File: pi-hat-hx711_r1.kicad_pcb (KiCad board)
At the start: 2 copper layers, 65 x 56 mm, 15 parts, among them J1 GPIO, J2 Conn_01x06, J5 Conn_01x06, Q1 S8550, U2 HX711, U3 TPS7A20xxxDQN

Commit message: loloxoxlxoxl
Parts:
- added C1: 100nF, Capacitor_SMD:C_0603_1608Metric, F.Cu at (133.9, 73.8)
- added U1: M24c64, Package_SO:SOIC-8_3.9x4.9mm_P1.27mm, F.Cu at (140.5, 58.9)
- moved R3 21.8 mm to (138.8, 53.5)
- moved R1 21.2 mm to (138.5, 51.5)
- moved U3 11.0 mm to (151.0, 67.2)

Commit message: lollll
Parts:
- added C3: 10uF, Capacitor_SMD:C_0805_2012Metric, F.Cu at (141.8, 67.3)
- added C4: 100nF, Capacitor_SMD:C_0603_1608Metric, F.Cu at (133.0, 59.1)
- added C5: 100nF, Capacitor_SMD:C_0603_1608Metric, F.Cu at (133.0, 61.7)
- added D1: SS14, Diode_SMD:D_SMA, F.Cu at (139.0, 60.2)
- added JP2: Jumper_2_Open, TestPoint:TestPoint_2Pads_Pitch2.54mm_Drill0.8mm, F.Cu at (136.8, 64.1)
- added L1: 4u7H, Inductor_SMD:L_Sunlord_SWPA3015S, F.Cu at (137.3, 68.1)
- added R5: 100k, Resistor_SMD:R_0603_1608Metric, F.Cu at (133.0, 64.2)
- added R6: 360k, Resistor_SMD:R_0603_1608Metric, F.Cu at (133.0, 66.7)
- added U4: TPS61040DBV, Package_TO_SOT_SMD:SOT-23-5, F.Cu at (149.8, 55.5)
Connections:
- Q1 pad 3: unconnected-(Q1-C-Pad3) -> +VDC
- U2 pad 3: unconnected-(U2-AVDD-Pad3) -> +VDC
- U2 pad 5: unconnected-(U2-AGND-Pad5) -> -VDC
- U2 pad 6: unconnected-(U2-VBG-Pad6) -> Net-(U2-VBG)

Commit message: rough blocking out the pcb
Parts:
- removed JP2: Jumper_2_Open, TestPoint:TestPoint_2Pads_Pitch2.54mm_Drill0.8mm
- added C10: 1uF, Capacitor_SMD:C_0603_1608Metric, F.Cu at (112.0, 61.0)
- added C11: 22uF, Capacitor_SMD:C_0805_2012Metric, F.Cu at (108.0, 57.5)
- added C12: 33pF, Capacitor_SMD:C_0603_1608Metric, F.Cu at (116.0, 53.5)
- added C6: 22uF, Capacitor_SMD:C_0805_2012Metric, F.Cu at (109.0, 67.5)
- added C7: 22uF, Capacitor_SMD:C_0805_2012Metric, F.Cu at (109.0, 65.5)
- added C8: 1uF, Capacitor_SMD:C_0603_1608Metric, F.Cu at (115.0, 67.0)
- added C9: 33pF, Capacitor_SMD:C_0603_1608Metric, F.Cu at (140.8, 68.5)
- added JP1: ID_WP, Jumper:SolderJumper-2_P1.3mm_Open_TrianglePad1.0x1.5mm, F.Cu at (158.0, 58.5)
- added JP3: SolderJumper_2_Open, Jumper:SolderJumper-2_P1.3mm_Open_TrianglePad1.0x1.5mm, F.Cu at (103.5, 57.5)
- added R10: 0R, Resistor_SMD:R_0603_1608Metric, F.Cu at (144.8, 68.5)
- added R11: 10k, Resistor_SMD:R_0603_1608Metric, F.Cu at (144.8, 71.0)
- added R12: 0R, Resistor_SMD:R_0603_1608Metric, F.Cu at (148.8, 61.0)
- added R13: 10k, Resistor_SMD:R_0603_1608Metric, F.Cu at (148.8, 63.5)
- added R14: 3k9, Resistor_SMD:R_0603_1608Metric, F.Cu at (148.8, 66.0)
- added R15: 0R, Resistor_SMD:R_0603_1608Metric, F.Cu at (148.8, 68.5)
- added R7: 1R, Resistor_SMD:R_0603_1608Metric, F.Cu at (109.0, 63.5)
- added R8: 0R, Resistor_SMD:R_0603_1608Metric, F.Cu at (144.8, 63.5)
- added R9: 0R, Resistor_SMD:R_0603_1608Metric, F.Cu at (144.8, 66.0)
- added TP1: TestPoint, TestPoint:TestPoint_THTPad_1.5x1.5mm_Drill0.7mm, F.Cu at (145.0, 74.0)
- added TP2: TestPoint, TestPoint:TestPoint_THTPad_1.5x1.5mm_Drill0.7mm, F.Cu at (97.5, 64.5)
- added TP3: TestPoint, TestPoint:TestPoint_THTPad_1.5x1.5mm_Drill0.7mm, F.Cu at (96.0, 69.5)
- U3: value TPS7A20xxxDQN -> TPS7A2050PDQNR
- moved U4 38.8 mm to (111.0, 57.5), turned to -90 degrees
- moved U3 38.5 mm to (112.5, 67.5), turned to 180 degrees
- moved Q1 37.8 mm to (153.3, 73.7)
- moved R1 25.3 mm to (163.0, 58.0), turned to 180 degrees
- moved R3 24.9 mm to (163.0, 59.5), turned to 180 degrees
- moved L1 24.5 mm to (115.0, 58.0), turned to 90 degrees
- moved C1 24.4 mm to (156.5, 64.5), turned to -90 degrees
- moved R6 22.8 mm to (116.0, 51.5), turned to 180 degrees
- moved R5 22.6 mm to (113.0, 53.5), turned to 180 degrees
- moved U1 20.9 mm to (160.5, 64.9)
- moved D1 20.6 mm to (118.5, 59.0), turned to 90 degrees
- moved C4 8.93 mm to (140.8, 63.5)
- moved C5 8.93 mm to (140.8, 66.0)
- moved C3 6.54 mm to (141.0, 73.8)
- moved U2 5.91 mm to (130.5, 74.0), turned to 90 degrees
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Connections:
- net /IN1+ renamed /Analog/IN1+
- net /IN1- renamed /Analog/IN1-
- C3 pad 2: unconnected-(C3-Pad2) -> GND
- C4 pad 2: unconnected-(C4-Pad2) -> GND
- C5 pad 2: -VDC -> GND
- D1 pad 1: unconnected-(D1-K-Pad1) -> /power/VBOOST
- D1 pad 2: unconnected-(D1-A-Pad2) -> Net-(D1-A)
- J2 pad 1: -VDC -> GND
- J2 pad 2: -VDC -> /REFIN1-
- J2 pad 5: +VDC -> /REFIN1+
- J5 pad 2: +VDC -> /REFIN1+
- J5 pad 5: -VDC -> /REFIN1-
- J5 pad 6: -VDC -> GND
- L1 pad 1: unconnected-(L1-Pad1) -> +5V
- L1 pad 2: unconnected-(L1-Pad2) -> Net-(D1-A)
- Q1 pad 2: +5V -> Net-(Q1-E)
- R5 pad 1: unconnected-(R5-Pad1) -> Net-(U4-FB)
- R5 pad 2: unconnected-(R5-Pad2) -> GND
- R6 pad 1: unconnected-(R6-Pad1) -> /power/VBOOST
- R6 pad 2: unconnected-(R6-Pad2) -> Net-(U4-FB)
- U2 pad 1: +5V -> VDDA
- U2 pad 11: unconnected-(U2-PD_SCK-Pad11) -> /GPIO11/SPI0.SCLK
- U2 pad 12: unconnected-(U2-DOUT-Pad12) -> /GPIO9/SPI0.MISO
- U2 pad 14: unconnected-(U2-XI-Pad14) -> Net-(U2-XI)
- U2 pad 15: unconnected-(U2-RATE-Pad15) -> Net-(U2-RATE)
- U2 pad 2: Net-(Q1-B) -> Net-(U2-BASE)
- U2 pad 4: unconnected-(U2-VFB-Pad4) -> Net-(U2-VFB)
- U2 pad 5: -VDC -> GND
- U3 pad 1: unconnected-(U3-OUT-Pad1) -> VDDA
- U3 pad 2: unconnected-(U3-GND-Pad2) -> GND
- U3 pad 3: unconnected-(U3-EN-Pad3) -> Net-(U3-EN)
- U3 pad 4: unconnected-(U3-IN-Pad4) -> Net-(U3-EN)
- U3 pad 5: unconnected-(U3-Pad-Pad5) -> GND
- U4 pad 1: unconnected-(U4-SW-Pad1) -> Net-(D1-A)
- U4 pad 2: unconnected-(U4-GND-Pad2) -> GND
- U4 pad 3: unconnected-(U4-FB-Pad3) -> Net-(U4-FB)
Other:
- copper layers 2 -> 4

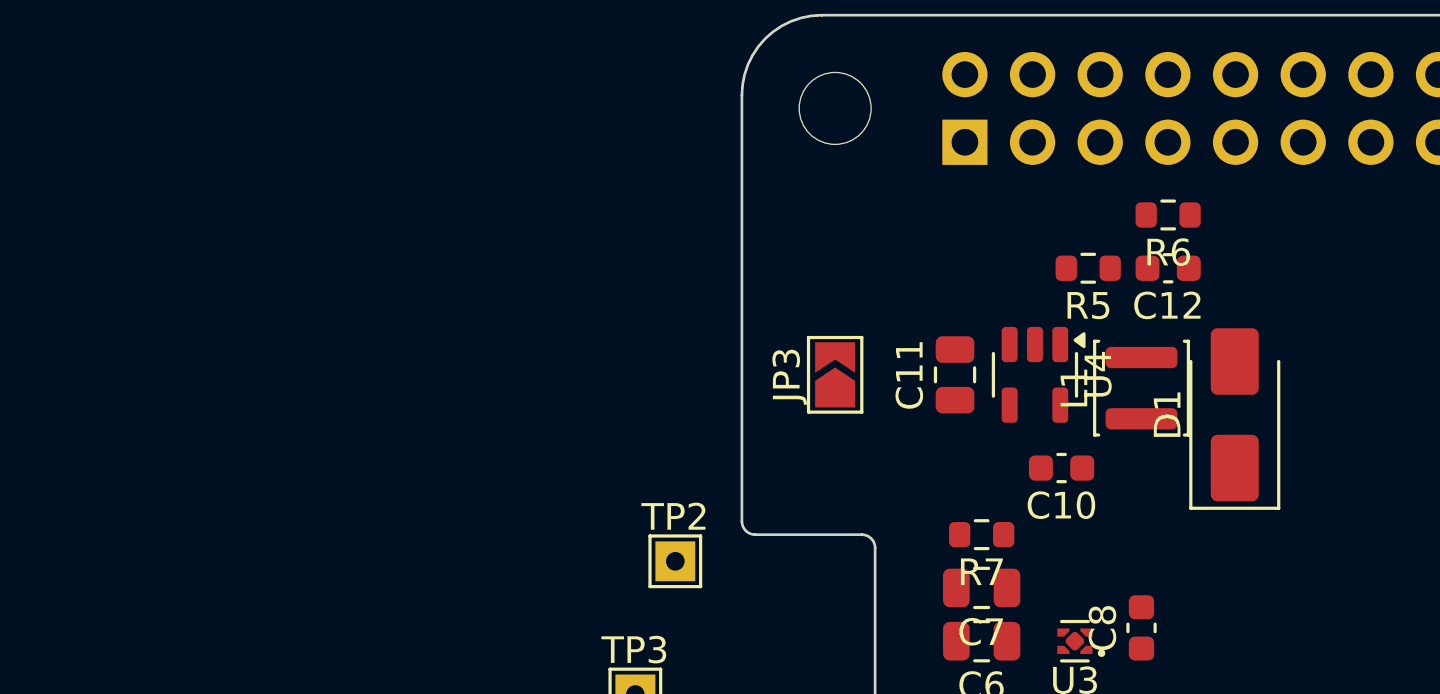
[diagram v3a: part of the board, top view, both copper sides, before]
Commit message: better parts, start pushing layout blocks
SMA is dumb, way too big
the swpa3030 was... unnecessarily small. we're trying to be super chill
power here, don't push it hot.  (Still, 1A was.. really, more than
enough? but 1A is a 40C rise, so.. let's just have less....)
use more caps too. why the fuck not. more filtering, more happy.

holy fuck though, kicad on wayland is giving me the shits!
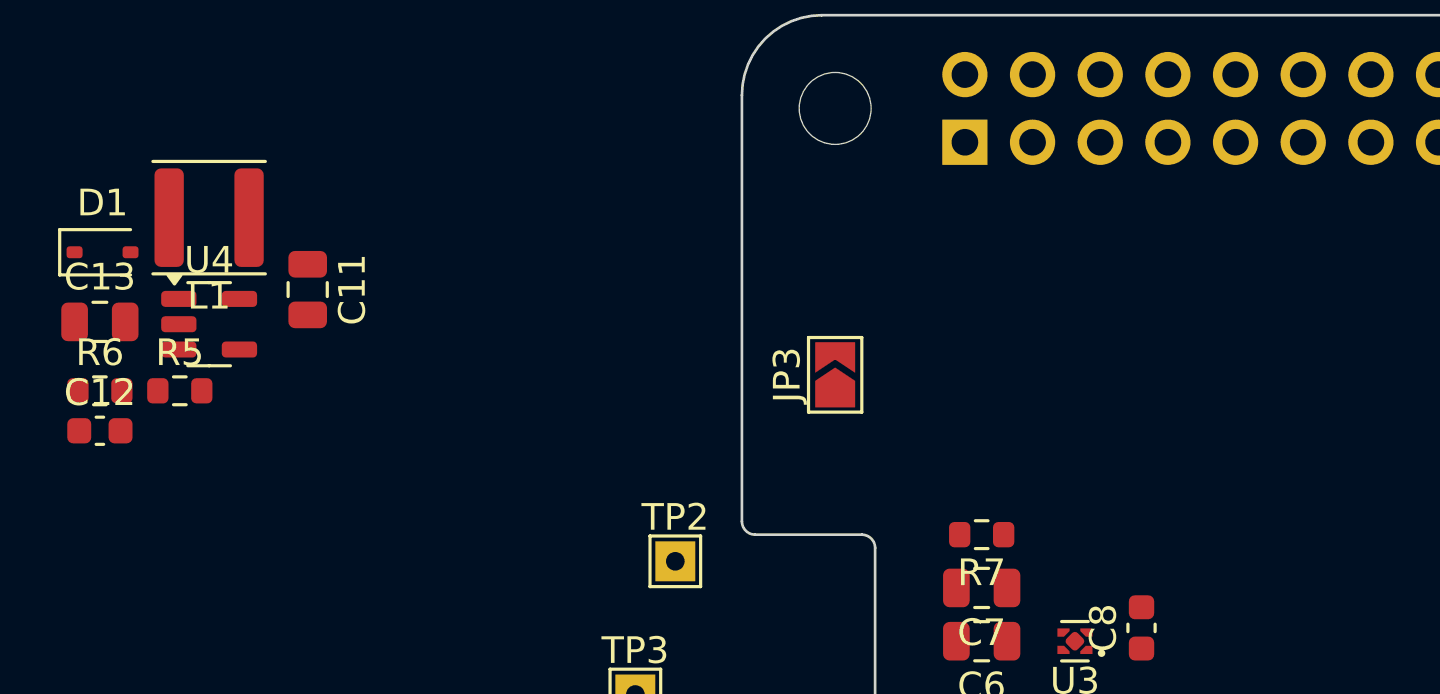
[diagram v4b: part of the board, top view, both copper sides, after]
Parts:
- removed C10: 1uF, Capacitor_SMD:C_0603_1608Metric
- added C13: 10uF, Capacitor_SMD:C_0805_2012Metric, F.Cu at (75.9, 55.5)
- D1: value SS14 -> 1N5819WS; footprint Diode_SMD:D_SMA -> Diode_SMD:D_SOD-323
- L1: footprint Inductor_SMD:L_Sunlord_SWPA3015S -> Inductor_SMD:L_Changjiang_FNR4030S
- moved D1 42.9 mm to (76.0, 52.9), turned to 0 degrees
- moved R6 40.6 mm to (75.9, 58.1), turned to 0 degrees
- moved C12 40.6 mm to (75.9, 59.6), turned to 0 degrees
- moved L1 35.6 mm to (80.0, 51.6), turned to 180 degrees
- moved R5 34.4 mm to (78.9, 58.1), turned to 0 degrees
- moved U4 31.1 mm to (80.0, 55.6), turned to 0 degrees
- moved C11 24.5 mm to (83.7, 54.3), turned to -90 degrees

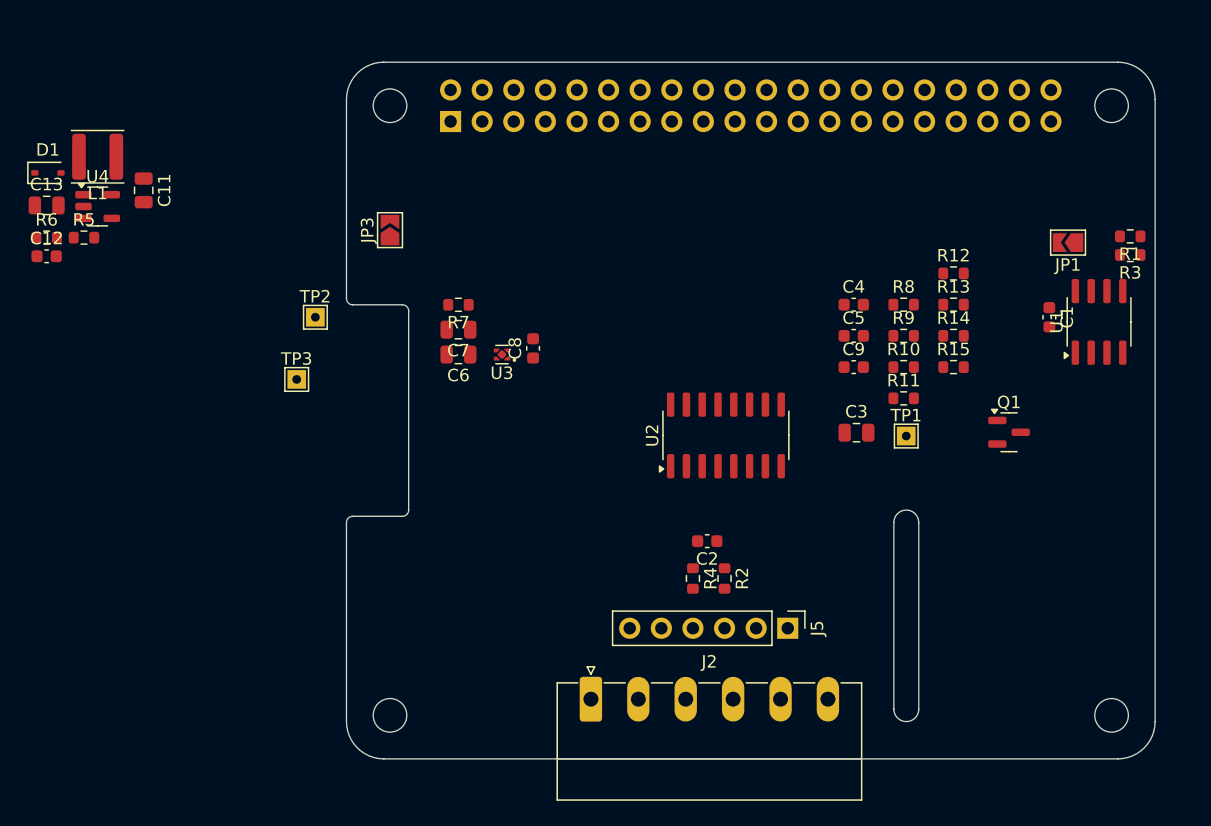
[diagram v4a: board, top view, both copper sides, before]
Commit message: add second channel input
switch to vertical connectors, so no concerns abotu edge space.
Allows offering the second channel, even though it's probably useless,
but it sets us up with a style we might be ok with for subsequent
boards.
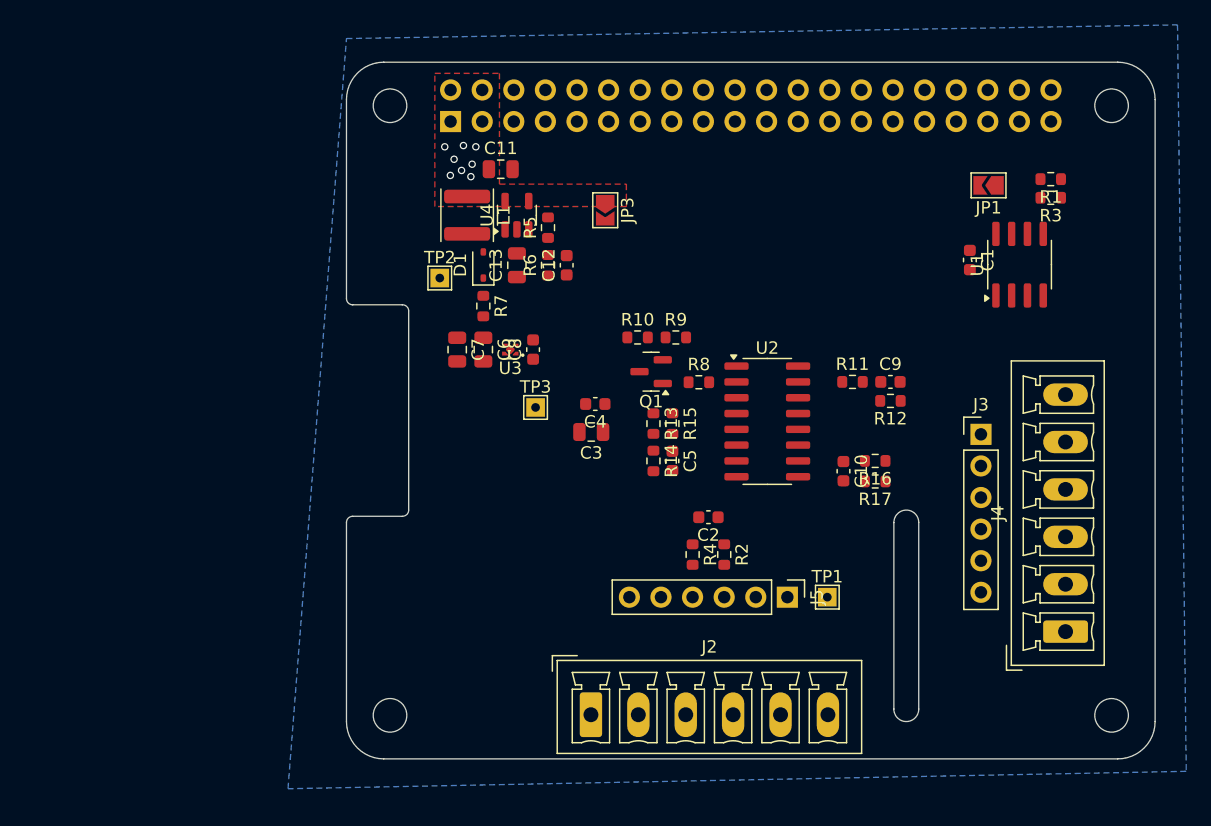
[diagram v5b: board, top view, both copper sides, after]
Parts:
- added C10: 100nF, Capacitor_SMD:C_0603_1608Metric, F.Cu at (139.9, 76.9)
- added J3: Conn_01x06, Connector_PinHeader_2.54mm:PinHeader_1x06_P2.54mm_Vertical, F.Cu at (151.0, 73.9)
- added J4: Conn_01x06, Connector_Phoenix_MC:PhoenixContact_MCV_1,5_6-G-3.81_1x06_P3.81mm_Vertical, F.Cu at (157.8, 89.8)
- added R16: 100R, Resistor_SMD:R_0603_1608Metric, F.Cu at (142.5, 76.0)
- added R17: 100R, Resistor_SMD:R_0603_1608Metric, F.Cu at (142.5, 77.7)
- J2: footprint Connector_Phoenix_MC:PhoenixContact_MC_1,5_6-G-3.81_1x06_P3.81mm_Horizontal -> Connector_Phoenix_MC:PhoenixContact_MCV_1,5_6-G-3.81_1x06_P3.81mm_Vertical
- moved C12 41.8 mm to (117.7, 60.3), turned to 90 degrees
- moved R6 40.4 mm to (116.2, 60.3), turned to 90 degrees
- moved C13 38.1 mm to (113.7, 60.3), turned to 90 degrees
- moved R5 37.3 mm to (116.2, 57.3), turned to 90 degrees
- moved D1 35.8 mm to (111.0, 60.3), turned to 90 degrees
- moved U4 33.7 mm to (113.7, 56.3), turned to 90 degrees
- moved L1 30.1 mm to (109.7, 56.3), turned to -90 degrees
- moved Q1 29.2 mm to (124.5, 68.9), turned to 180 degrees
- moved C11 28.8 mm to (112.4, 52.6), turned to 0 degrees
- moved R14 26.1 mm to (124.7, 76.0), turned to -90 degrees
- moved R13 25.9 mm to (124.7, 73.0), turned to -90 degrees
- moved R15 23.0 mm to (126.2, 73.0), turned to -90 degrees
- moved C4 22.3 mm to (120.0, 71.5), turned to 180 degrees
- moved R10 21.5 mm to (123.4, 66.1)
- moved C3 21.3 mm to (119.7, 73.7), turned to 180 degrees
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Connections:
- net +VDC renamed /EXE1+
- U2 pad 10: unconnected-(U2-INB+-Pad10) -> /BR_OUT2+
- U2 pad 9: unconnected-(U2-INB--Pad9) -> /BR_OUT2-
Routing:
- net +5V: vias 0 -> 8
- added copper zone on In2.Cu, net +3V3
- added copper zone on F.Cu, net +5V
- added copper zone on In2.Cu, net +5V
- added copper zone on B.Cu, net GND
- added copper zone on In1.Cu, net GND
- added copper zone on In2.Cu, net VDDA

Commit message: pushing blocks
roughyl how we want it?
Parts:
- added TP4: TestPoint, TestPoint:TestPoint_THTPad_1.5x1.5mm_Drill0.7mm, F.Cu at (103.3, 52.5)
- moved TP3 15.9 mm to (104.0, 60.5)
- moved TP2 6.14 mm to (103.8, 56.5)
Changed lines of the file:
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@@
 	(footprint "TestPoint:TestPoint_THTPad_1.5x1.5mm_Drill0.7mm"
 		(layer "F.Cu")
-		(at 107.5 61.35)
+		(at 103.8 56.45)
 		(descr "THT rectangular pad as test Point, square 1.5mm side length, hole diameter 0.7mm")
 		(tags "test point THT pad rectangle square")
@@
 	(footprint "TestPoint:TestPoint_THTPad_1.5x1.5mm_Drill0.7mm"
 		(layer "F.Cu")
-		(at 115.2 71.75)
+		(at 104 60.5)
 		(descr "THT rectangular pad as test Point, square 1.5mm side length, hole diameter 0.7mm")
 		(tags "test point THT pad rectangle square")
@@
 		)
 	)
+	(footprint "TestPoint:TestPoint_THTPad_1.5x1.5mm_Drill0.7mm"
+		(layer "F.Cu")
+		(at 103.3 52.5)
+		(descr "THT rectangular pad as test Point, square 1.5mm side length, hole diameter 0.7mm")
+		(tags "test point THT pad rectangle square")
+		(property "Reference" "TP4"
+			(at 0 -1.648 0)
+			(layer "F.SilkS")
+			(effects
+				(font
+					(size 1 1)
+					(thickness 0.15)
+				)
+			)
+		)
+		(property "Value" "TestPoint"
+			(at 0 1.75 0)
+			(layer "F.Fab")
+			(effects
+				(font
+					(size 1 1)
+					(thickness 0.15)
+				)
+			)
+		)
+		(property "Datasheet" "~"
+			(at 0 0 0)
+			(unlocked yes)
+			(layer "F.Fab")
+			(hide yes)
+			(effects
+				(font
+					(size 1.27 1.27)
+					(thickness 0.15)
+				)
+			)
+		)
+		(property "Description" "test point"
+			(at 0 0 0)
+			(unlocked yes)
+			(layer "F.Fab")
+			(hide yes)
+			(effects
+				(font
+					(size 1.27 1.27)
+					(thickness 0.15)
+				)
+			)
+		)
+		(property ki_fp_filters "Pin* Test*")
+		(sheetname "/power/")
+		(sheetfile "power.kicad_sch")
+		(attr exclude_from_pos_files)
+		(fp_line
+			(start -0.95 -0.95)
+			(end 0.95 -0.95)
+			(stroke
+				(width 0.12)
+				(type solid)
+			)
+			(layer "F.SilkS")
+		)
+		(fp_line
+			(start -0.95 0.95)
+			(end -0.95 -0.95)
+			(stroke
+				(width 0.12)
+				(type solid)
+			)
+			(layer "F.SilkS")
+		)
+		(fp_line
+			(start 0.95 -0.95)
+			(end 0.95 0.95)
+			(stroke
+				(width 0.12)
+				(type solid)
+			)
+			(layer "F.SilkS")
+		)
+		(fp_line
+			(start 0.95 0.95)
+			(end -0.95 0.95)
+			(stroke
+				(width 0.12)
+				(type solid)
+			)
+			(layer "F.SilkS")
+		)
+		(fp_line
+			(start -1.25 -1.25)
+			(end -1.25 1.25)
+			(stroke
+				(width 0.05)
+				(type solid)
+			)
+			(layer "F.CrtYd")
+		)
+		(fp_line
+			(start -1.25 -1.25)
+			(end 1.25 -1.25)
+			(stroke
+				(width 0.05)
+				(type solid)
+			)
+			(layer "F.CrtYd")
+		)
+		(fp_line
+			(start 1.25 1.25)
+			(end -1.25 1.25)
+			(stroke
+				(width 0.05)
+				(type solid)
+			)
+			(layer "F.CrtYd")
+		)
+		(fp_line
+			(start 1.25 1.25)
+			(end 1.25 -1.25)
+			(stroke
+				(width 0.05)
+				(type solid)
+			)
+			(layer "F.CrtYd")
+		)
+		(fp_text user "${REFERENCE}"
+			(at 0 -1.65 0)
+			(layer "F.Fab")
+			(effects
+				(font
+					(size 1 1)
+					(thickness 0.15)
+				)
+			)
+		)
+		(pad "1" thru_hole rect
+			(at 0 0)
+			(size 1.5 1.5)
+			(drill 0.7)
+			(layers "*.Cu" "*.Mask")
+			(remove_unused_layers no)
+			(net 1 "GND")
+			(pinfunction "1")
+			(pintype "passive")
+		)
+		(embedded_fonts no)
+	)
 	(footprint "Package_TO_SOT_SMD:SOT-23-5"
